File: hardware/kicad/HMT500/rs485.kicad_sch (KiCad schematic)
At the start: 2 parts, among them U11 THVD2450DR

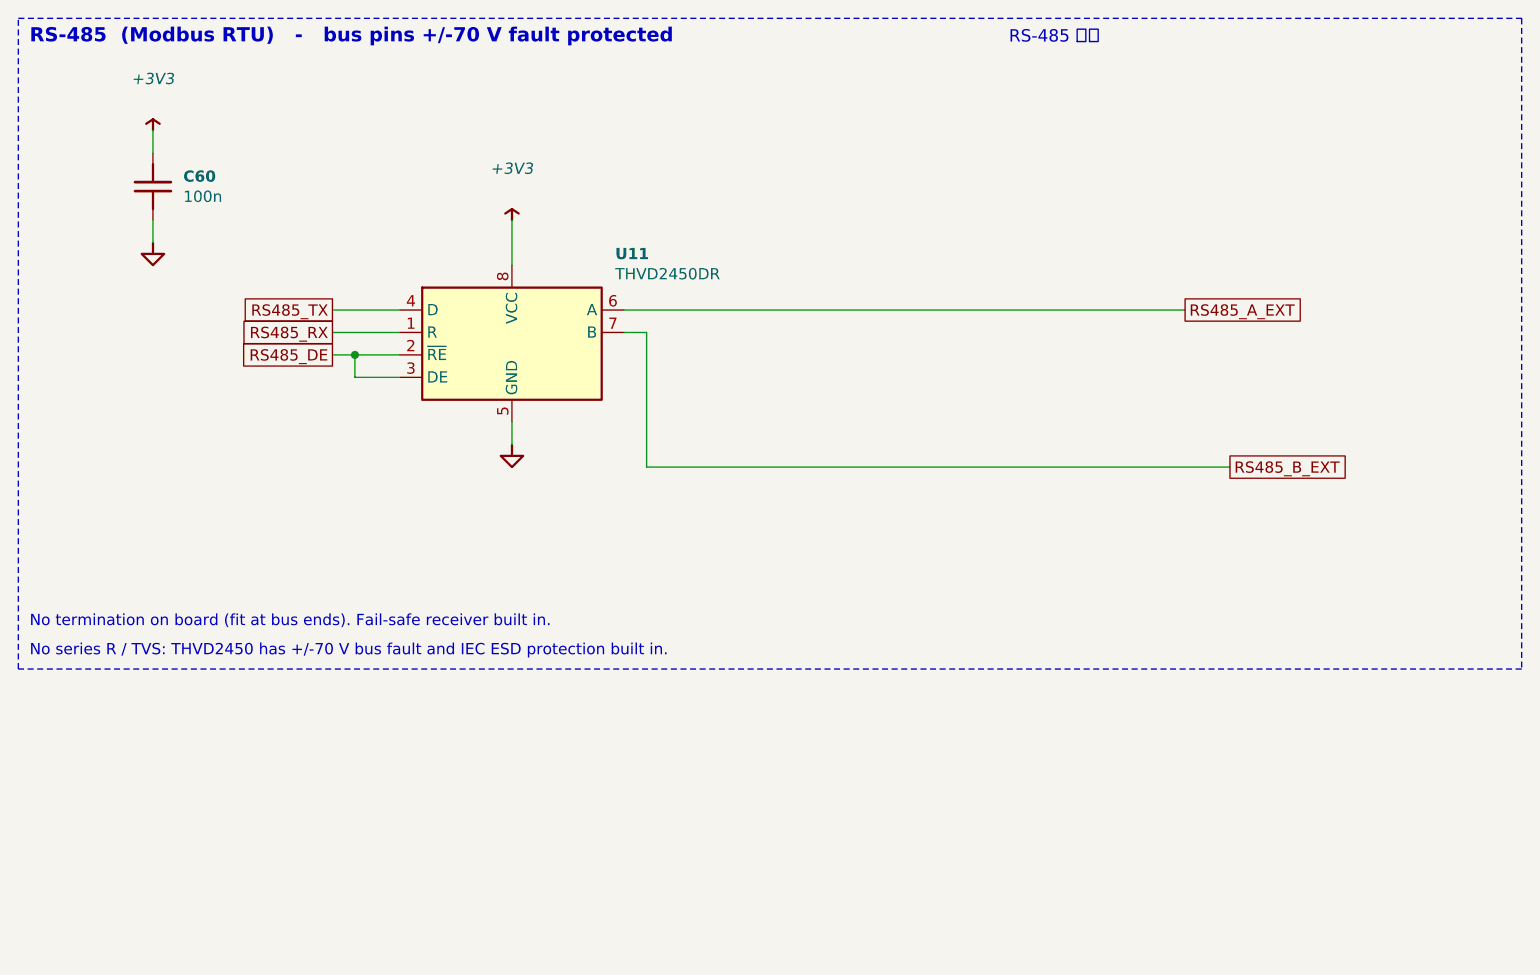
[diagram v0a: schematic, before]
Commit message: Schematic redraw: aligned parts, straight wires, fewer junctions
- Bends 54 -> 1, junctions 51 -> 31 (remaining are real 3-way nodes: divider taps,
  protection taps, tied pin pairs, power flags)
- Power pins get their own power symbols instead of rails with T-branches; signals
  between distant parts use labels; two-pin parts sit on the pin row they connect to
- Symbol pin order rearranged for straight runs (pin numbers unchanged): TPS2660,
  LMR36006 (BOOT on top), PCAP04 (Cref pins 3 rows apart, VDD18 on right), ADS1220
  (bottom pins 3 apart), DAC8760 (GND-tied pins on bottom), TPS26611 (FLT on bottom)
- New checks: pin names inside IC bodies must not overlap, boxes must not overlap;
  test limits bends per sheet and total junctions
- Netlist check 63 nets, 0 errors

Co-Authored-By: Claude Opus 5.5 <noreply@anthropic.com>
Claude-Session: https://claude.ai/code/session_01JA2o8uJsqp9Vzsg4b665ev
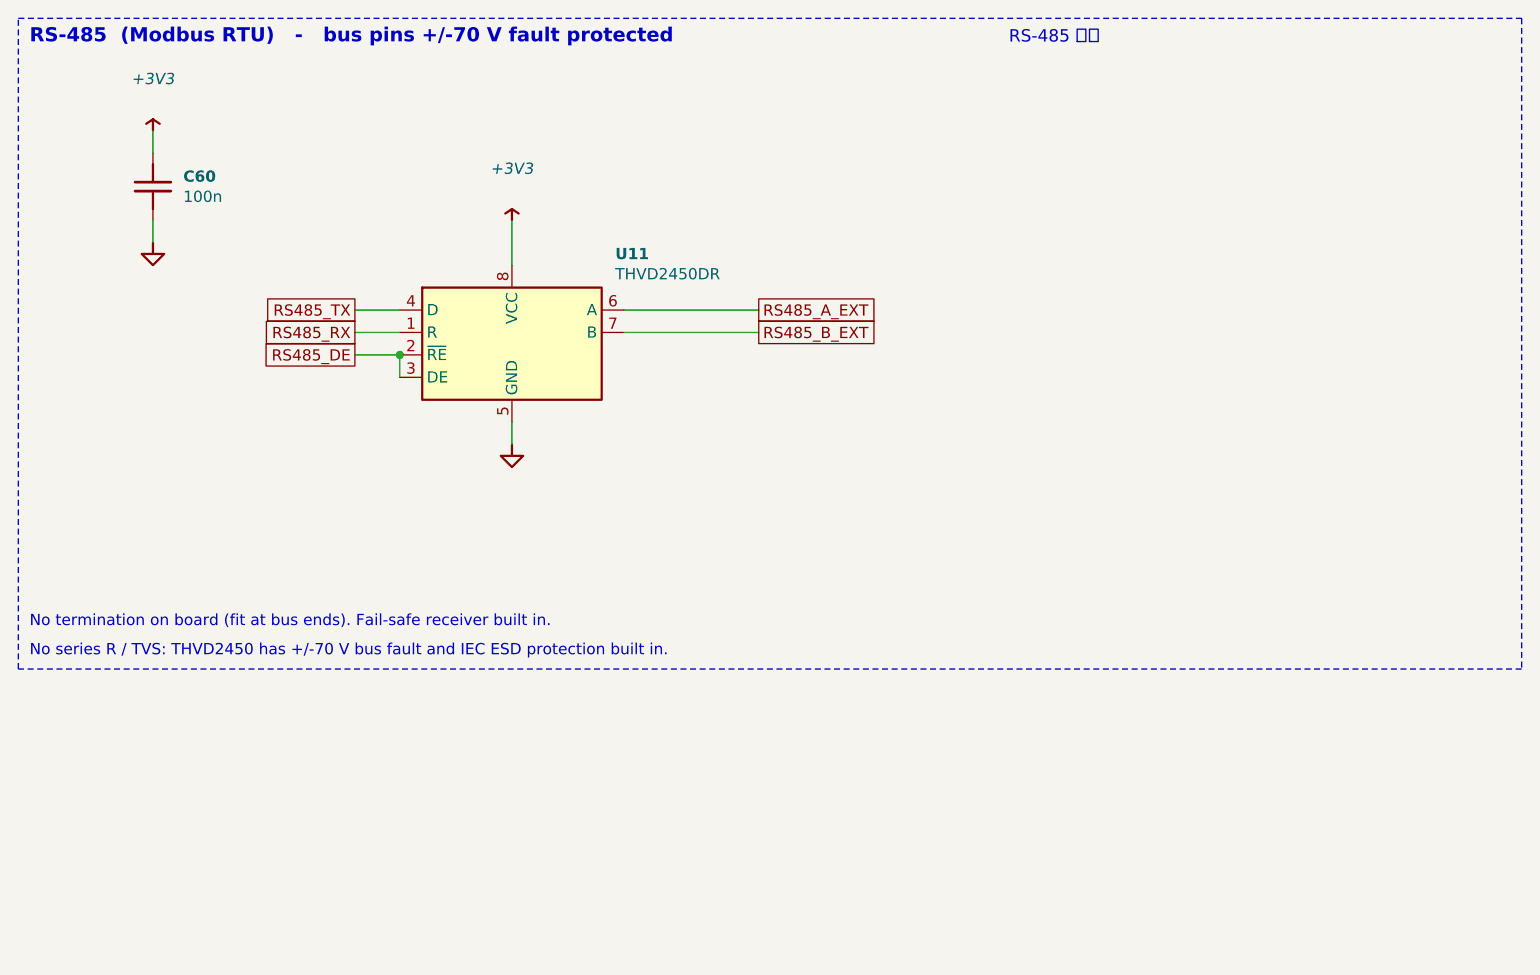
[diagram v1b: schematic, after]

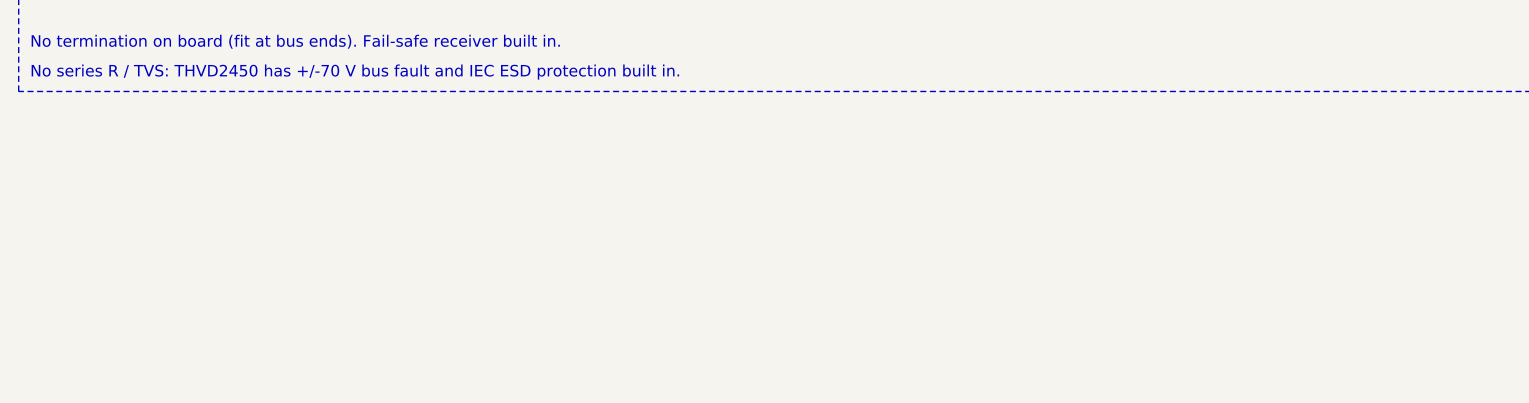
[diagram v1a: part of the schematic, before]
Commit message: Schematic: key-parts table (role, features, specs) on every sheet
- Aligned 4-column table per sheet: reference, part, role, features/specs;
  values still to confirm against datasheets marked with *
- Connector and RS-485 sheets moved to A3 for room
- New checks: text and boxes stay inside the page and out of the title block;
  every character of Hangul text must exist in NanumGothic (minus sign and micro
  sign substituted)

Co-Authored-By: Claude Opus 5.5 <noreply@anthropic.com>
Claude-Session: https://claude.ai/code/session_01JA2o8uJsqp9Vzsg4b665ev
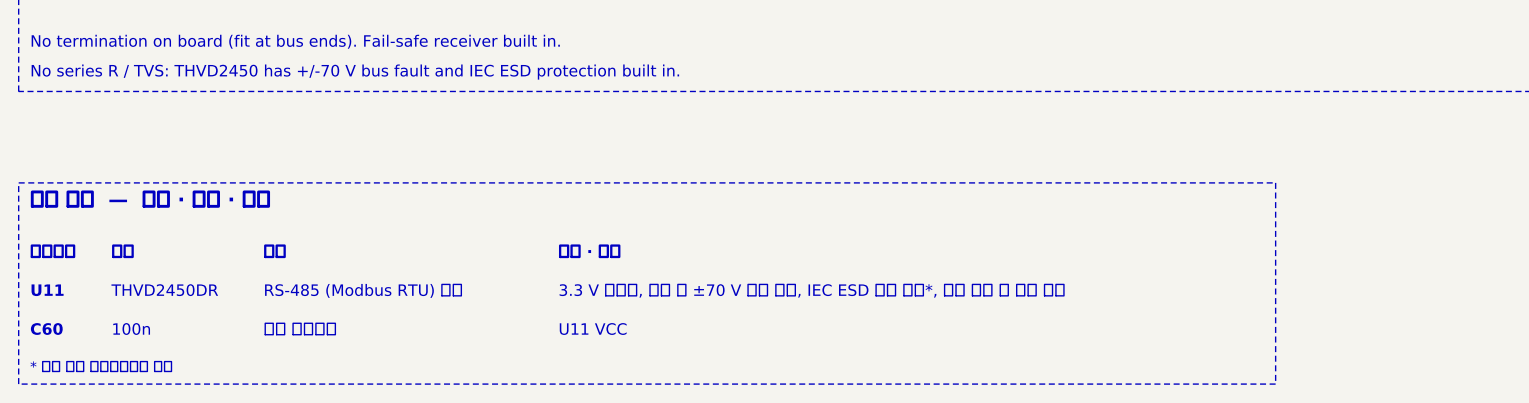
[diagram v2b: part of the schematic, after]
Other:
- note added: "* 표시 값은 데이터시트로 확인"
- note added: "100n"
- note added: "3.3 V 반이중, 버스 핀 ±70 V 고장 보호, IEC ESD 보호 내장*, 버스 개방 시 안전 수신"
- note added: "C60"
- note added: "RS-485 (Modbus RTU) 통신"
- note added: "THVD2450DR"
- note added: "U11"
- note added: "U11 VCC"
- note added: "부품"
- note added: "부품번호"
- note added: "역할"
- note added: "전원 바이패스"
- note added: "주요 부품 — 역할 · 특징 · 사양"
- note added: "특징 · 사양"
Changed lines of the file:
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@@
-(kicad_sch (version 20230121) (generator eeschema) (paper "A4")
+(kicad_sch (version 20230121) (generator eeschema) (paper "A3")
 (title_block (title "HMT500  RS-485") (date "2026-09-29") (rev "0.6") (company "DOTECH Co., Ltd.") (comment 1 "Oil moisture transmitter HMT500 - RS-485 + 2x V/I analog output") (comment 2 "Design notes: docs/hw/circuit-design.md") (comment 3 "VERIFY=YES parts: pin numbers LMR36006/PCAP04/DAC8760/TPS26611; TPS2660 R22"))
 (symbol (lib_id "HMT500:THVD2450") (at 86.36 63.5 0) (unit 1) (in_bom yes) (on_board yes) (dnp no) (property "Reference" "U11" (at 98.044 54.61 0) (effects (font (size 1.27 1.27) bold) (justify left))) (property "Value" "THVD2450DR" (at 98.044 56.896 0) (effects (font (size 1.27 1.27)) (justify left))) (property "Footprint" "Package_SO:SOIC-8_3.9x4.9mm_P1.27mm" (at 86.36 63.5 0) (effects (font (size 1.27 1.27)) hide)) (property "Datasheet" "~" (at 86.36 63.5 0) (effects (font (size 1.27 1.27)) hide)) (pin "4") (pin "1") (pin "2") (pin "3") (pin "6") (pin "7") (pin "8") (pin "5") (instances (project "HMT500" (path "/1ebb025b-11bd-5f7c-aaab-41e2a750e8b3/45f1df26-d453-5179-997b-24dddad436e5" (reference "U11") (unit 1)))))
@@
 (junction (at 73.66 66.04) (diameter 0) (color 0 0 0 0))
 (rectangle (start 30.48 27.94) (end 200.66 101.6) (stroke (width 0.1524) (type dash) (color 72 72 160 1)) (fill (type none)))
+(rectangle (start 30.48 111.76) (end 170.142 134.112) (stroke (width 0.1524) (type dash) (color 72 72 160 1)) (fill (type none)))
 (text "RS-485  (Modbus RTU)   -   bus pins +/-70 V fault protected" (at 31.75 30.988 0) (effects (font (size 1.6 1.6) bold) (justify left bottom)))
 (text "RS-485 통신" (at 142.61 30.988 0) (effects (font (face "NanumGothic") (size 1.4 1.4)) (justify left bottom)))
 (text "No termination on board (fit at bus ends). Fail-safe receiver built in." (at 31.75 97.028 0) (effects (font (size 1.27 1.27)) (justify left bottom)))
 (text "No series R / TVS: THVD2450 has +/-70 V bus fault and IEC ESD protection built in." (at 31.75 100.33 0) (effects (font (size 1.27 1.27)) (justify left bottom)))
+(text "부품번호" (at 31.75 120.396 0) (effects (font (face "NanumGothic") (size 1.27 1.27) bold) (justify left bottom)))
+(text "부품" (at 40.7924 120.396 0) (effects (font (face "NanumGothic") (size 1.27 1.27) bold) (justify left bottom)))
+(text "역할" (at 57.6834 120.396 0) (effects (font (face "NanumGothic") (size 1.27 1.27) bold) (justify left bottom)))
+(text "특징 · 사양" (at 90.4494 120.396 0) (effects (font (face "NanumGothic") (size 1.27 1.27) bold) (justify left bottom)))
+(text "U11" (at 31.75 124.714 0) (effects (font (size 1.27 1.27) bold) (justify left bottom)))
+(text "THVD2450DR" (at 40.7924 124.714 0) (effects (font (size 1.27 1.27)) (justify left bottom)))
+(text "RS-485 (Modbus RTU) 통신" (at 57.6834 124.714 0) (effects (font (face "NanumGothic") (size 1.27 1.27)) (justify left bottom)))
+(text "3.3 V 반이중, 버스 핀 ±70 V 고장 보호, IEC ESD 보호 내장*, 버스 개방 시 안전 수신" (at 90.4494 124.714 0) (effects (font (face "NanumGothic") (size 1.27 1.27)) (justify left bottom)))
+(text "C60" (at 31.75 129.032 0) (effects (font (size 1.27 1.27) bold) (justify left bottom)))
+(text "100n" (at 40.7924 129.032 0) (effects (font (size 1.27 1.27)) (justify left bottom)))
+(text "전원 바이패스" (at 57.6834 129.032 0) (effects (font (face "NanumGothic") (size 1.27 1.27)) (justify left bottom)))
+(text "U11 VCC" (at 90.4494 129.032 0) (effects (font (size 1.27 1.27)) (justify left bottom)))
+(text "주요 부품  —  역할 · 특징 · 사양" (at 31.75 114.808 0) (effects (font (face "NanumGothic") (size 1.6 1.6) bold) (justify left bottom)))
+(text "* 표시 값은 데이터시트로 확인" (at 31.75 133.096 0) (effects (font (face "NanumGothic") (size 1.1 1.1)) (justify left bottom)))
 )
